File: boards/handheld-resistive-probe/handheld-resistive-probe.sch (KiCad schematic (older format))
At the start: 4 parts, among them J1 Conn_Coaxial, J2 Conn_01x01

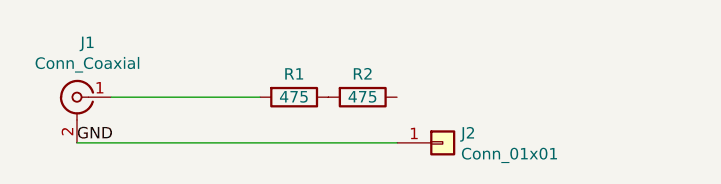
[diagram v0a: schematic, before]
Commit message: handheld-resistive-probe: respin with coplanar waveguide PCB layout
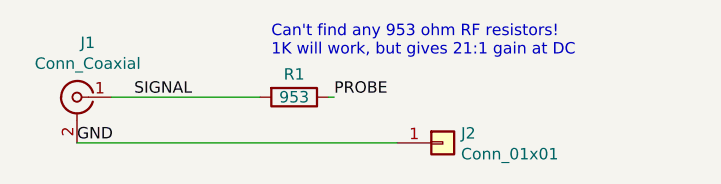
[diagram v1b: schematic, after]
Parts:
- removed R2: 475, azonenberg_pcb:EIA_0402_RES_NOSILK, symbol device:R
- R1: value 475 -> 953
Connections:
- net PROBE: now reaches R1.1
- net SIGNAL: now reaches J1.1 (In), R1.2
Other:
- note added: "Can't find any 953 ohm RF resistors!\n1K will work, but gives 21:1 gain at DC"
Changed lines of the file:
@@
-EESchema Schematic File Version 4
+EESchema Schematic File Version 5
 LIBS:handheld-resistive-probe-cache
 EELAYER 29 0
@@
 Sheet 1 1
 Title "Handheld 20:1 Z0 probe"
-Date "2019-04-16"
+Date "2019-05-09"
 Rev "0.1"
 Comp "Antikernel Labs"
@@
 P 5450 3200
 F 0 "R1" V 5350 3200 50  0000 C CNN
-F 1 "475" V 5450 3200 50  0000 C CNN
+F 1 "953" V 5450 3200 50  0000 C CNN
 F 2 "azonenberg_pcb:EIA_0402_RES_NOSILK" V 5380 3200 50  0001 C CNN
 F 3 "" H 5450 3200 50  0001 C CNN
 	1    5450 3200
-	0    1    1    0
-$EndComp
-$Comp
-L device:R R2
-U 1 1 5CB66FF9
-P 5750 3200
-F 0 "R2" V 5650 3200 50  0000 C CNN
-F 1 "475" V 5750 3200 50  0000 C CNN
-F 2 "azonenberg_pcb:EIA_0402_RES_NOSILK" V 5680 3200 50  0001 C CNN
-F 3 "" H 5750 3200 50  0001 C CNN
-	1    5750 3200
 	0    1    1    0
 $EndComp
@@
 Wire Wire Line
 	4500 3400 5900 3400
+Text Label 5625 3200 0    50   ~ 0
+PROBE
+Text Label 4750 3200 0    50   ~ 0
+SIGNAL
+Wire Wire Line
+	5625 3200 5600 3200
+Text Notes 5350 3025 0    50   ~ 0
+Can't find any 953 ohm RF resistors!\n1K will work, but gives 21:1 gain at DC
 $EndSCHEMATC

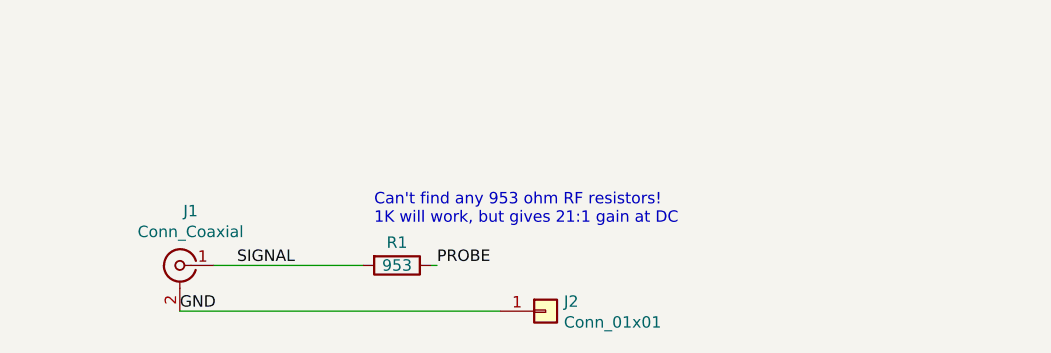
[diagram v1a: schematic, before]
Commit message: New rev of handheld-resistive-probe with five resistors to reduce parasitics
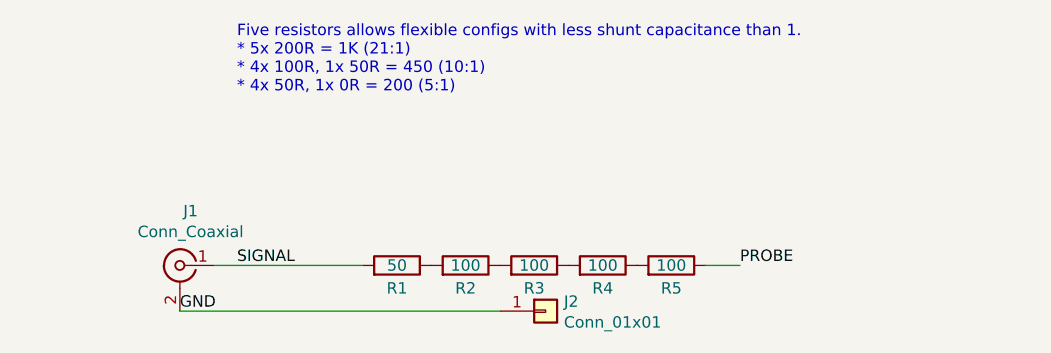
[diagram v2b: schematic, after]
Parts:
- added R2, R3, R4, R5: 100, azonenberg_pcb:EIA_0402_RES_NOSILK, symbol device:R
- R1: value 953 -> 50
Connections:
- net PROBE: now also R5.1; no longer R1.1
- new net: R1.1, R2.2
- new net: R2.1, R3.2
- new net: R3.1, R4.2
- new net: R4.1, R5.2
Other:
- note added: "Five resistors allows flexible configs with less shunt capacitance than 1.\n* 5x 200R = 1K (21:1)\n* 4x 100R, 1x 50R = 450 (10:1)\n* 4x 50R, 1x 0R = 200 (5:1)"
- note removed: "Can't find any 953 ohm RF resistors!\n1K will work, but gives 21:1 gain at DC"
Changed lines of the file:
@@
 Sheet 1 1
 Title "Handheld 20:1 Z0 probe"
-Date "2019-05-09"
-Rev "0.1"
+Date "2019-06-18"
+Rev "0.3"
 Comp "Antikernel Labs"
 Comment1 ""
@@
 Comment4 ""
 $EndDescr
-$Comp
-L device:R R1
-U 1 1 5CB66BBA
-P 5450 3200
-F 0 "R1" V 5350 3200 50  0000 C CNN
-F 1 "953" V 5450 3200 50  0000 C CNN
-F 2 "azonenberg_pcb:EIA_0402_RES_NOSILK" V 5380 3200 50  0001 C CNN
-F 3 "" H 5450 3200 50  0001 C CNN
-	1    5450 3200
-	0    1    1    0
-$EndComp
 $Comp
 L Connector:Conn_Coaxial J1
@@
 Wire Wire Line
 	4500 3400 5900 3400
-Text Label 5625 3200 0    50   ~ 0
+Text Label 6950 3200 0    50   ~ 0
 PROBE
 Text Label 4750 3200 0    50   ~ 0
 SIGNAL
+Text Notes 4750 2450 0    50   ~ 0
+Five resistors allows flexible configs with less shunt capacitance than 1.\n* 5x 200R = 1K (21:1)\n* 4x 100R, 1x 50R = 450 (10:1)\n* 4x 50R, 1x 0R = 200 (5:1)
+$Comp
+L device:R R2
+U 1 1 5D097CEB
+P 5750 3200
+F 0 "R2" V 5650 3200 50  0000 C CNN
+F 1 "100" V 5750 3200 50  0000 C CNN
+F 2 "azonenberg_pcb:EIA_0402_RES_NOSILK" V 5680 3200 50  0001 C CNN
+F 3 "" H 5750 3200 50  0001 C CNN
+	1    5750 3200
+	0    1    -1   0
+$EndComp
+$Comp
+L device:R R1
+U 1 1 5CB66BBA
+P 5450 3200
+F 0 "R1" V 5350 3200 50  0000 C CNN
+F 1 "50" V 5450 3200 50  0000 C CNN
+F 2 "azonenberg_pcb:EIA_0402_RES_NOSILK" V 5380 3200 50  0001 C CNN
+F 3 "" H 5450 3200 50  0001 C CNN
+	1    5450 3200
+	0    1    -1   0
+$EndComp
+$Comp
+L device:R R3
+U 1 1 5D098F11
+P 6050 3200
+F 0 "R3" V 5950 3200 50  0000 C CNN
+F 1 "100" V 6050 3200 50  0000 C CNN
+F 2 "azonenberg_pcb:EIA_0402_RES_NOSILK" V 5980 3200 50  0001 C CNN
+F 3 "" H 6050 3200 50  0001 C CNN
+	1    6050 3200
+	0    1    -1   0
+$EndComp
+$Comp
+L device:R R4
+U 1 1 5D099302
+P 6350 3200
+F 0 "R4" V 6250 3200 50  0000 C CNN
+F 1 "100" V 6350 3200 50  0000 C CNN
+F 2 "azonenberg_pcb:EIA_0402_RES_NOSILK" V 6280 3200 50  0001 C CNN
+F 3 "" H 6350 3200 50  0001 C CNN
+	1    6350 3200
+	0    1    -1   0
+$EndComp
+$Comp
+L device:R R5
+U 1 1 5D099902
+P 6650 3200
+F 0 "R5" V 6550 3200 50  0000 C CNN
+F 1 "100" V 6650 3200 50  0000 C CNN
+F 2 "azonenberg_pcb:EIA_0402_RES_NOSILK" V 6580 3200 50  0001 C CNN
+F 3 "" H 6650 3200 50  0001 C CNN
+	1    6650 3200
+	0    1    -1   0
+$EndComp
 Wire Wire Line
-	5625 3200 5600 3200
-Text Notes 5350 3025 0    50   ~ 0
-Can't find any 953 ohm RF resistors!\n1K will work, but gives 21:1 gain at DC
+	6800 3200 6950 3200
 $EndSCHEMATC

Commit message: Added distributed-element compensation cap for v0.4
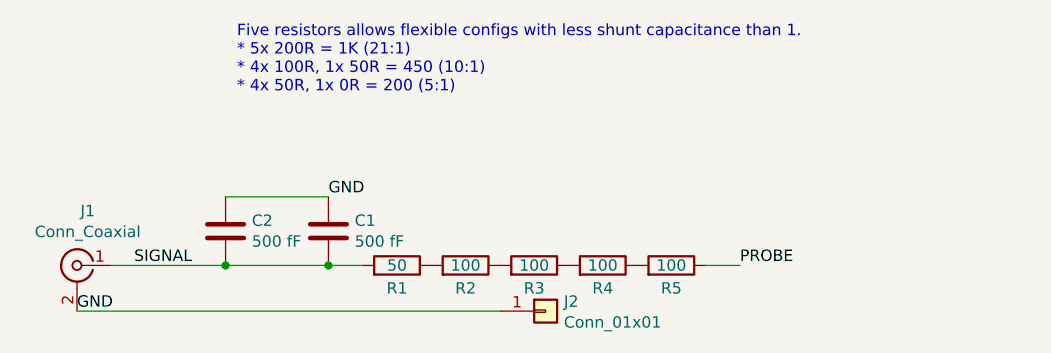
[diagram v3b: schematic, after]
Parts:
- added C1, C2: 500 fF, azonenberg_pcb:CAP_MICROSTRIP_0p5PF, symbol device:C
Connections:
- net GND: now also C1.1, C2.1
- net SIGNAL: now also C1.2, C2.2
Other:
- moved on the sheet: J1
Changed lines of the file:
@@
 Sheet 1 1
 Title "Handheld 20:1 Z0 probe"
-Date "2019-06-18"
-Rev "0.3"
+Date "2019-06-21"
+Rev "0.4"
 Comp "Antikernel Labs"
 Comment1 ""
@@
 L Connector:Conn_Coaxial J1
 U 1 1 5CB67590
-P 4500 3200
-F 0 "J1" H 4453 3438 50  0000 C CNN
-F 1 "Conn_Coaxial" H 4453 3347 50  0000 C CNN
-F 2 "azonenberg_pcb:CONN_MMCX_J_P_H_ST_EM1" H 4500 3200 50  0001 C CNN
-F 3 "" H 4500 3200 50  0001 C CNN
-	1    4500 3200
+P 4050 3200
+F 0 "J1" H 4003 3438 50  0000 C CNN
+F 1 "Conn_Coaxial" H 4003 3347 50  0000 C CNN
+F 2 "azonenberg_pcb:CONN_MMCX_J_P_H_ST_EM1" H 4050 3200 50  0001 C CNN
+F 3 "" H 4050 3200 50  0001 C CNN
+	1    4050 3200
 	-1   0    0    -1
 $EndComp
 Wire Wire Line
-	4650 3200 5300 3200
-Text Label 4500 3400 0    50   ~ 0
+	4200 3200 4700 3200
+Text Label 4050 3400 0    50   ~ 0
 GND
 $Comp
@@
 	1    0    0    -1
 $EndComp
-Wire Wire Line
-	4500 3400 5900 3400
 Text Label 6950 3200 0    50   ~ 0
 PROBE
-Text Label 4750 3200 0    50   ~ 0
+Text Label 4300 3200 0    50   ~ 0
 SIGNAL
 Text Notes 4750 2450 0    50   ~ 0
@@
 Wire Wire Line
 	6800 3200 6950 3200
+$Comp
+L device:C C1
+U 1 1 5D0D656F
+P 5150 3050
+F 0 "C1" H 5265 3096 50  0000 L CNN
+F 1 "500 fF" H 5265 3005 50  0000 L CNN
+F 2 "azonenberg_pcb:CAP_MICROSTRIP_0p5PF" H 5188 2900 50  0001 C CNN
+F 3 "" H 5150 3050 50  0001 C CNN
+	1    5150 3050
+	1    0    0    -1
+$EndComp
+Wire Wire Line
+	5150 3200 5300 3200
+Text Label 5150 2900 0    50   ~ 0
+GND
+Wire Wire Line
+	4050 3400 5900 3400
+$Comp
+L device:C C2
+U 1 1 5D0D837E
+P 4700 3050
+F 0 "C2" H 4815 3096 50  0000 L CNN
+F 1 "500 fF" H 4815 3005 50  0000 L CNN
+F 2 "azonenberg_pcb:CAP_MICROSTRIP_0p5PF" H 4738 2900 50  0001 C CNN
+F 3 "" H 4700 3050 50  0001 C CNN
+	1    4700 3050
+	1    0    0    -1
+$EndComp
+Wire Wire Line
+	5150 2900 4700 2900
+Wire Wire Line
+	5150 3200 4700 3200
+Connection ~ 5150 3200
+Connection ~ 4700 3200
 $EndSCHEMATC
